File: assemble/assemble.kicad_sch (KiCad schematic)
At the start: 110 parts, among them J1 Conn_02x04_Odd_Even, SW1 SW_Push, SW10 SW_Push, SW11 SW_Push, SW12 SW_Push, SW13 SW_Push, SW14 SW_Push, SW15 SW_Push, SW16 SW_Push, SW17 SW_Push, SW18 SW_Push, SW19 SW_Push, SW2 SW_Push, SW20 SW_Push, SW21 SW_Push, SW22 SW_Push, SW23 SW_Push, SW24 SW_Push, SW25 SW_Push, SW26 SW_Push, SW27 SW_Push, SW28 SW_Push, SW29 SW_Push, SW3 SW_Push, SW30 SW_Push, SW31 SW_Push, SW32 SW_Push, SW33 SW_Push, SW34 SW_Push, SW35 SW_Push, SW36 SW_Push, SW37 SW_Push, SW38 SW_Push, SW39 SW_Push, SW4 SW_Push, SW40 SW_Push, SW41 SW_Push, SW42 SW_Push, SW43 SW_SPDT, SW44 SW_SPDT, SW45 RotaryEncoder_Switch, SW5 SW_Push, SW6 SW_Push, SW7 SW_Push, SW8 SW_Push, SW9 SW_Push, U1 XIAO-nRF52840-SMD, U2 XIAO-nRF52840-SMD

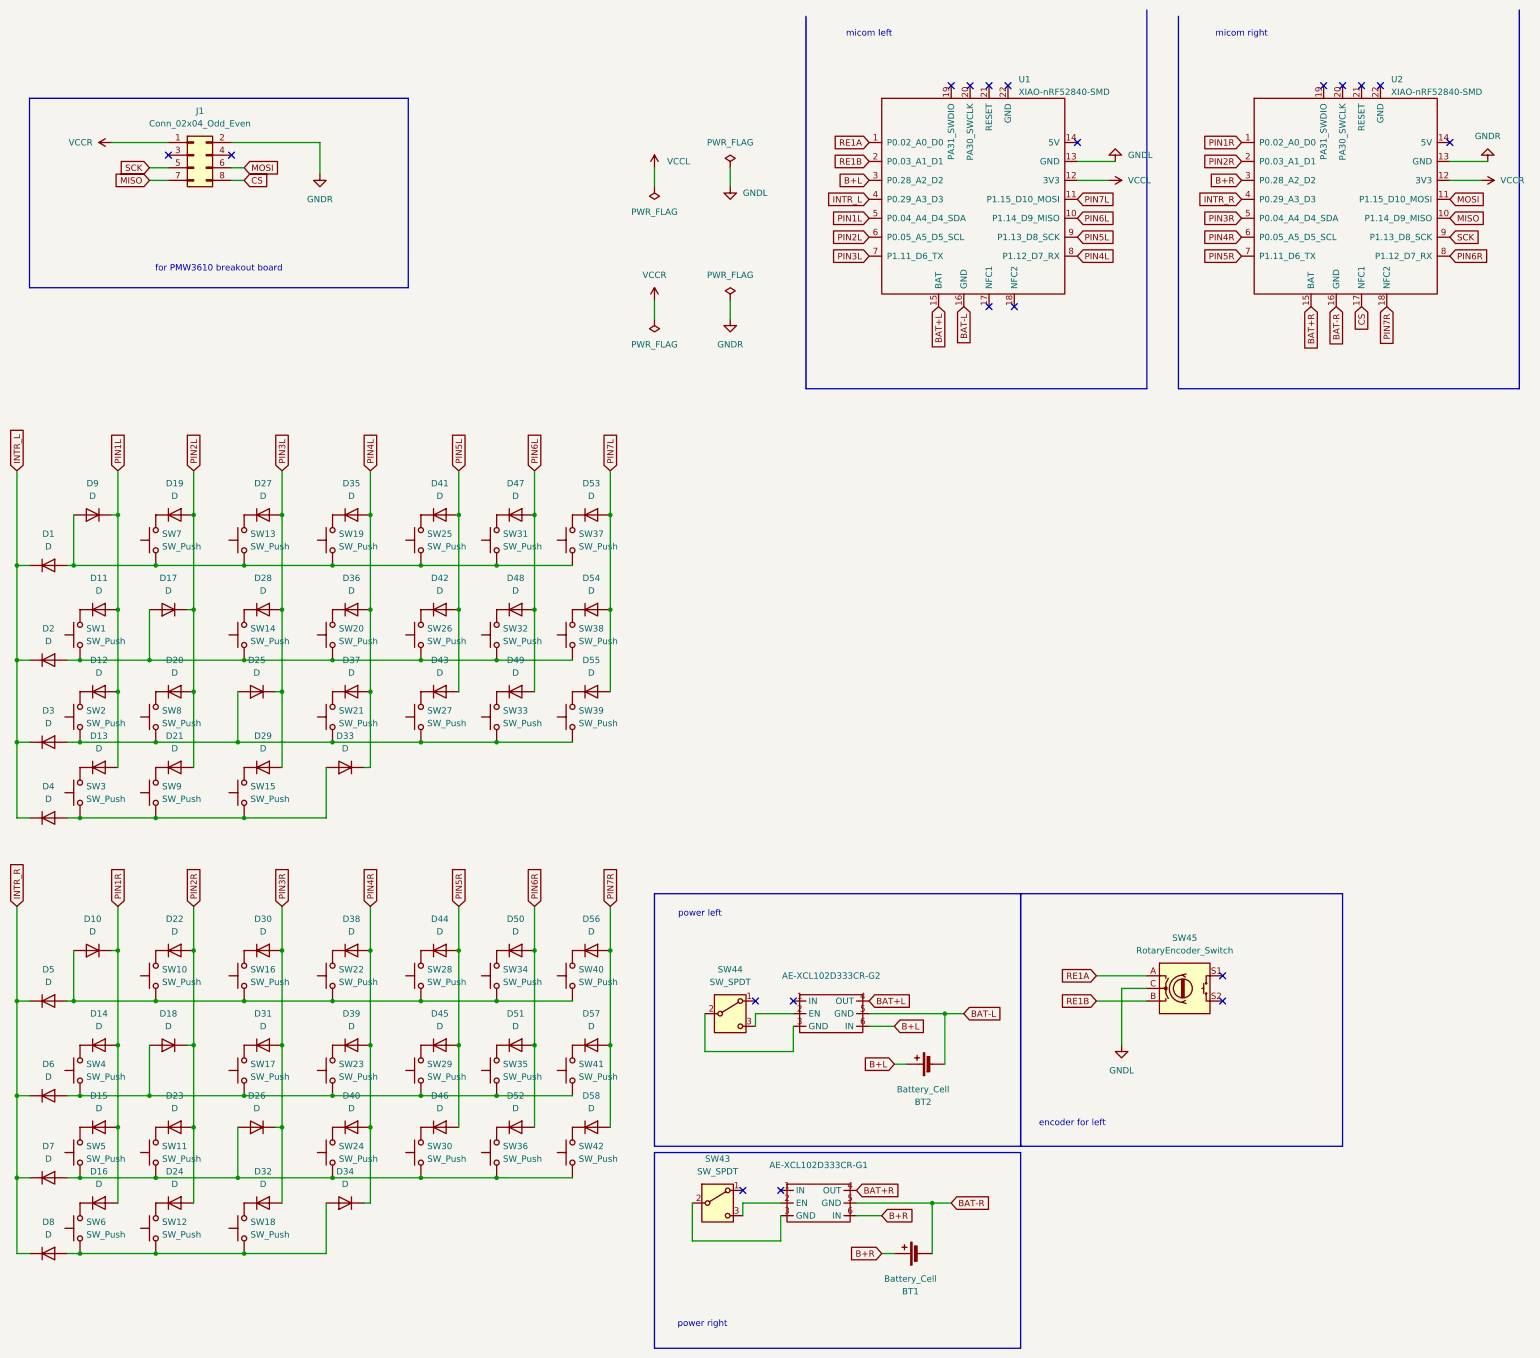
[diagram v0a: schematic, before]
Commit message: feat: add some rotary encoder
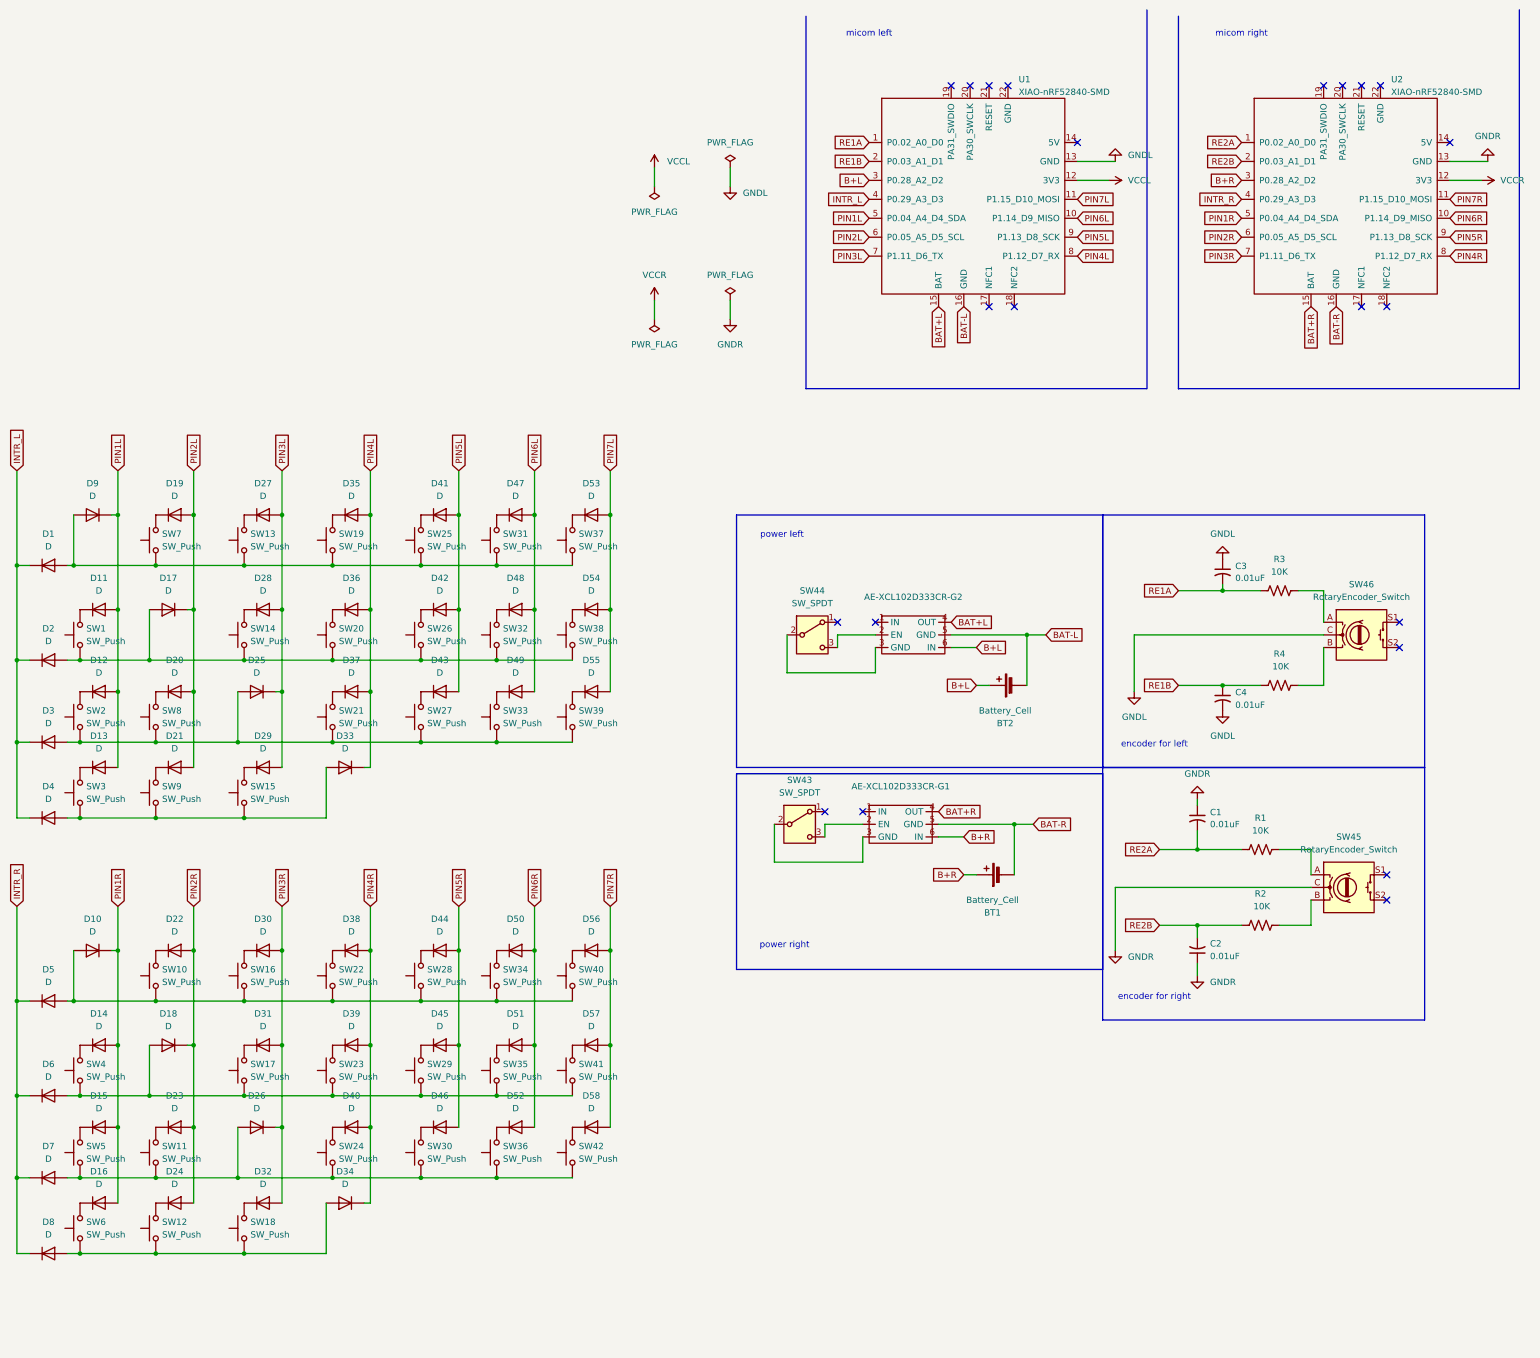
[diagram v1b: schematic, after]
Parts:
- removed J1: Conn_02x04_Odd_Even, Connector_PinSocket_2.54mm:PinSocket_2x04_P2.54mm_Vertical, symbol Connector_Generic:Conn_02x04_Odd_Even
- added C1, C2, C3, C4: 0.01uF, symbol Device:C_Small_US
- added R1, R2, R3, R4: 10K, symbol Device:R_US
- added SW45: RotaryEncoder_Switch, kbd_Parts:RotaryEncoder_EC12E, symbol Device:RotaryEncoder_Switch
- renumbered SW45 to SW46
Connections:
- net MISO is gone; now on net PIN6R: U2.10 (P1.14_D9_MISO)
- net MOSI is gone; now on net PIN7R: U2.11 (P1.15_D10_MOSI)
- net SCK is gone; now on net PIN5R: U2.9 (P1.13_D8_SCK)
- net GNDL: now also C3.1, C4.2
- net GNDR: now also C1.1, C2.1, SW45.C
- net PIN1R: now also U2.5 (P0.04_A4_D4_SDA); no longer U2.1 (P0.02_A0_D0)
- net PIN2R: now also U2.6 (P0.05_A5_D5_SCL); no longer U2.2 (P0.03_A1_D1)
- net PIN3R: now also U2.7 (P1.11_D6_TX); no longer U2.5 (P0.04_A4_D4_SDA)
- net PIN4R: now also U2.8 (P1.12_D7_RX); no longer U2.6 (P0.05_A5_D5_SCL)
- net PIN5R: no longer U2.7 (P1.11_D6_TX)
- net PIN6R: no longer U2.8 (P1.12_D7_RX)
- net PIN7R: no longer U2.18 (NFC2)
- net RE1A: now also C3.2, R3.1; no longer SW46.A
- net RE1B: now also C4.1, R4.1; no longer SW46.B
- net CS: no longer names the net of U2.17 (NFC1)
- new net: R2.2, SW45.B
- new net: R3.2, SW46.A
- new net: R4.2, SW46.B
- new net: R1.2, SW45.A
- new net RE2A: C1.2, R1.1, U2.1 (P0.02_A0_D0)
- new net RE2B: C2.2, R2.1, U2.2 (P0.03_A1_D1)
- no-connect marks 20 -> 22
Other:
- note added: "encoder for right"
- note removed: "for PMW3610 breakout board"
- moved on the sheet: AE-XCL102D333CR-G1, AE-XCL102D333CR-G2, BT1, BT2, SW43, SW44, SW46

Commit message: wip: implement PCB
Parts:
- added BT3, BT4: Battery_Cell, kbd_Parts:Battery_AAA, symbol Device:Battery_Cell
- added J1, J3: Conn_01x04, Connector_JST:JST_ZH_B4B-ZR_1x04_P1.50mm_Vertical, symbol Connector_Generic:Conn_01x04
- added J2, J4: Conn_01x04, Connector_Wire:SolderWire-0.5sqmm_1x04_P4.6mm_D0.9mm_OD2.1mm, symbol Connector_Generic:Conn_01x04
- BT1, BT2: footprint Battery:BatteryHolder_Keystone_2460_1xAA -> kbd_Parts:Battery_AAA
- C1, C2, C3, C4: footprint (none) -> kbd_Parts:Capacitor_1206
- R1, R2, R3, R4: footprint (none) -> Resistor_SMD:R_0805_2012Metric_Pad1.20x1.40mm_HandSolder
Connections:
- net B+L: now also J1.1 (Pin_1); no longer BT2.1 (+)
- net B+R: now also J3.1 (Pin_1); no longer BT1.1 (+)
- net at SW43.2 (B): now also J4.4 (Pin_4); no longer AE-XCL102D333CR-G1.3 (GND)
- net at SW43.3 (C): now also J4.3 (Pin_3); no longer AE-XCL102D333CR-G1.2 (EN)
- net at SW44.3 (C): now also J2.3 (Pin_3); no longer AE-XCL102D333CR-G2.2 (EN)
- net at SW44.2 (B): now also J2.4 (Pin_4); no longer AE-XCL102D333CR-G2.3 (GND)
- net BAT-L renamed B-L
- net B-L: now also J1.2 (Pin_2); no longer BT2.2 (-)
- net BAT-R renamed B-R
- net B-R: now also J3.2 (Pin_2); no longer BT1.2 (-)
- new net: BT3.1 (+), J4.1 (Pin_1)
- new net: BT1.2 (-), J4.2 (Pin_2)
- new net: BT1.1 (+), BT3.2 (-)
- new net: BT4.1 (+), J2.1 (Pin_1)
- new net: BT2.2 (-), J2.2 (Pin_2)
- new net: BT2.1 (+), BT4.2 (-)
- new net: AE-XCL102D333CR-G2.2 (EN), J1.4 (Pin_4)
- new net: AE-XCL102D333CR-G2.3 (GND), J1.3 (Pin_3)
- new net: AE-XCL102D333CR-G1.3 (GND), J3.3 (Pin_3)
- new net: AE-XCL102D333CR-G1.2 (EN), J3.4 (Pin_4)
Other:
- moved on the sheet: AE-XCL102D333CR-G2, BT1, BT2, SW43, SW44
